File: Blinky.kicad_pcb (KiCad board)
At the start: 2 copper layers, 35.6 x 26.7 mm, 7 parts, among them U1 7555

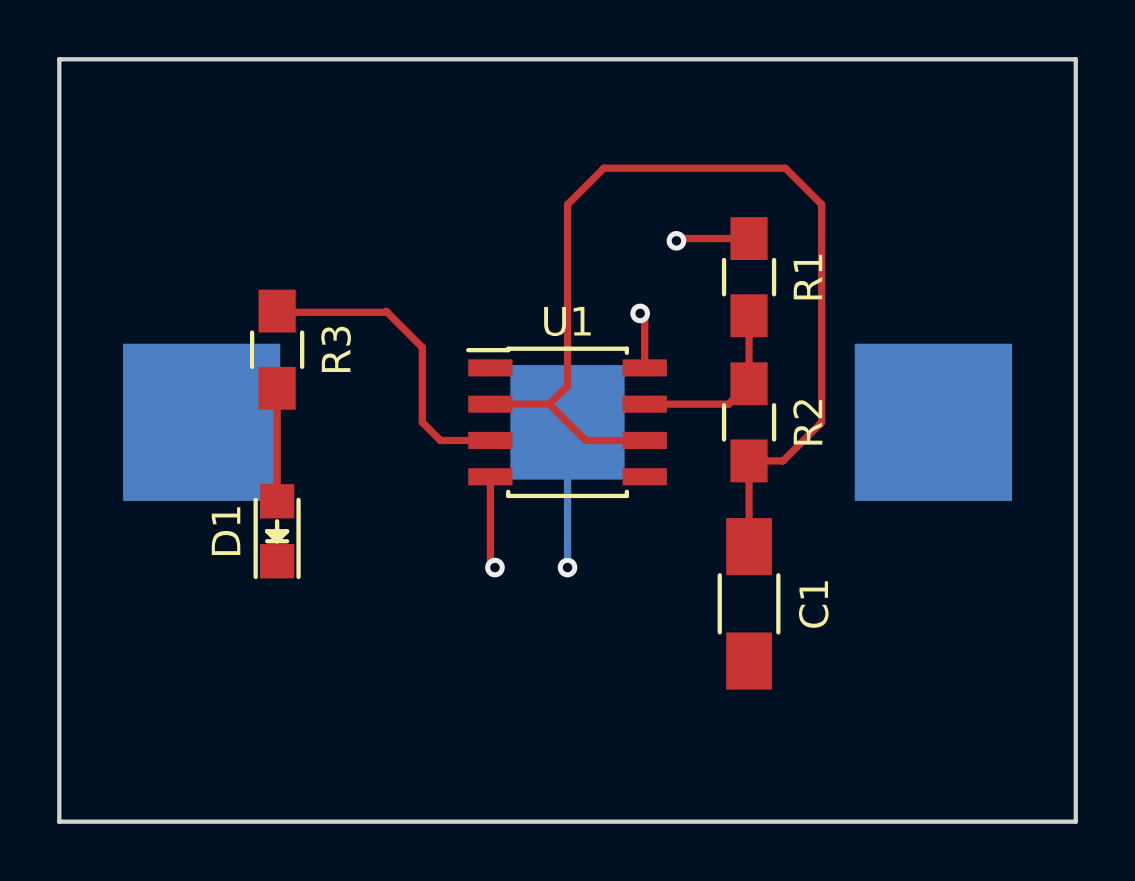
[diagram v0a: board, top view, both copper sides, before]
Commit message: Fix capacitor footprint - should have been 0805
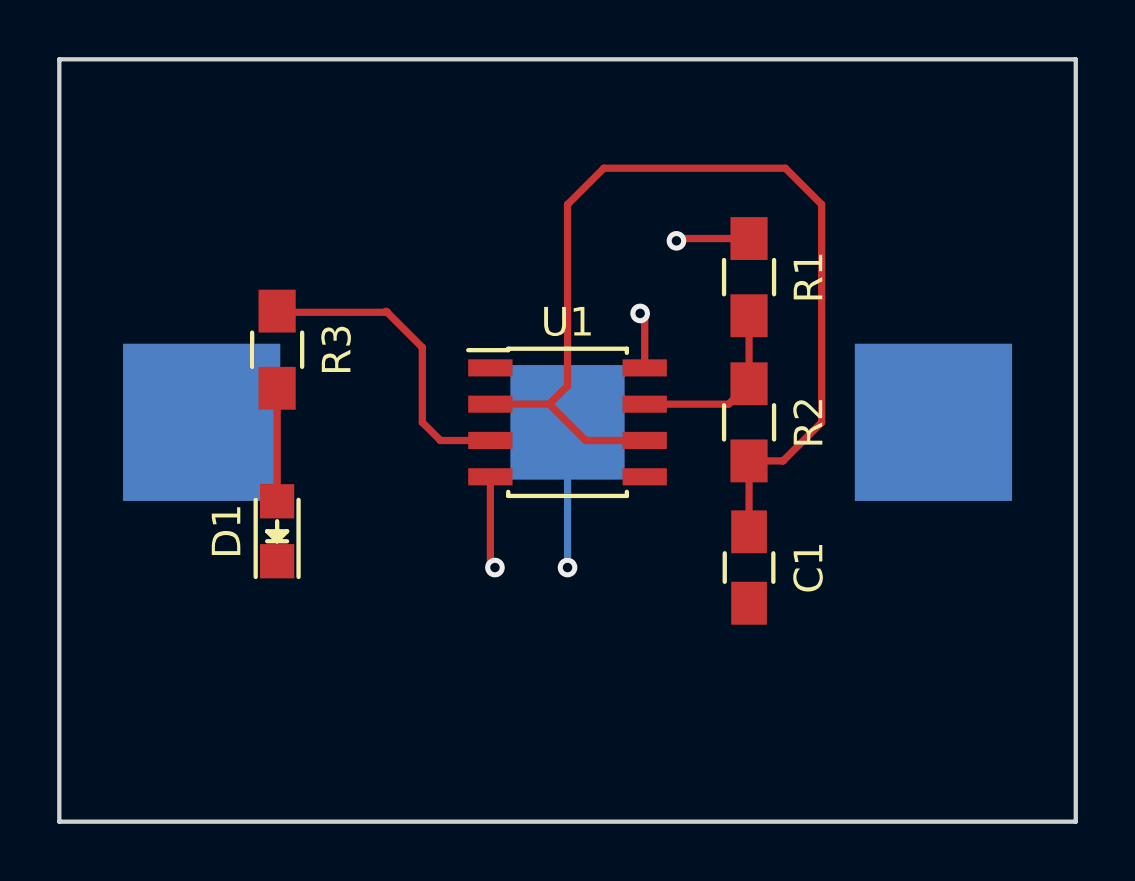
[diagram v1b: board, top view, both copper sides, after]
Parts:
- C1: footprint Capacitors_SMD:C_1206_HandSoldering -> Capacitors_SMD:C_0805_HandSoldering
- moved C1 1.27 mm to (162.6, 123.2)
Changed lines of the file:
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@@
   (layers
     (0 F.Cu mixed)
-    (31 B.Cu mixed)
+    (31 B.Cu mixed hide)
     (32 B.Adhes user)
     (33 F.Adhes user)
@@
     (add_net "Net-(U1-Pad5)")
   )
-  (module Capacitors_SMD:C_1206_HandSoldering (layer F.Cu)
-    (at 162.56 124.46 270)
-    (descr "Capacitor SMD 1206, hand soldering")
-    (tags "capacitor 1206")
-    (attr smd)
-    (fp_text reference C1 (at 0 -2.3 270) (layer F.SilkS)
-      (effects (font (size 1 1) (thickness 0.15)))
-    )
-    (fp_text value 1U (at 0 2.3 270) (layer F.Fab)
-      (effects (font (size 1 1) (thickness 0.15)))
-    )
-    (fp_line (start -3.3 -1.15) (end 3.3 -1.15) (layer F.CrtYd) (width 0.05))
-    (fp_line (start -3.3 1.15) (end 3.3 1.15) (layer F.CrtYd) (width 0.05))
-    (fp_line (start -3.3 -1.15) (end -3.3 1.15) (layer F.CrtYd) (width 0.05))
-    (fp_line (start 3.3 -1.15) (end 3.3 1.15) (layer F.CrtYd) (width 0.05))
-    (fp_line (start 1 -1.025) (end -1 -1.025) (layer F.SilkS) (width 0.15))
-    (fp_line (start -1 1.025) (end 1 1.025) (layer F.SilkS) (width 0.15))
-    (pad 1 smd rect (at -2 0 270) (size 2 1.6) (layers F.Cu F.Paste F.Mask)
-      (net 1 "Net-(C1-Pad1)"))
-    (pad 2 smd rect (at 2 0 270) (size 2 1.6) (layers F.Cu F.Paste F.Mask)
-      (net 2 GND))
-    (model Capacitors_SMD.3dshapes/C_1206_HandSoldering.wrl
-      (at (xyz 0 0 0))
-      (scale (xyz 1 1 1))
-      (rotate (xyz 0 0 0))
-    )
-  )
   (module LEDs:LED_0805 (layer F.Cu)
     (at 146.05 121.92 90)
@@
       (net 4 /VDD))
   )
+  (module Capacitors_SMD:C_0805_HandSoldering (layer F.Cu)
+    (at 162.56 123.19 270)
+    (descr "Capacitor SMD 0805, hand soldering")
+    (tags "capacitor 0805")
+    (attr smd)
+    (fp_text reference C1 (at 0 -2.1 270) (layer F.SilkS)
+      (effects (font (size 1 1) (thickness 0.15)))
+    )
+    (fp_text value 1U (at 0 2.1 270) (layer F.Fab)
+      (effects (font (size 1 1) (thickness 0.15)))
+    )
+    (fp_line (start -1 0.625) (end -1 -0.625) (layer F.Fab) (width 0.15))
+    (fp_line (start 1 0.625) (end -1 0.625) (layer F.Fab) (width 0.15))
+    (fp_line (start 1 -0.625) (end 1 0.625) (layer F.Fab) (width 0.15))
+    (fp_line (start -1 -0.625) (end 1 -0.625) (layer F.Fab) (width 0.15))
+    (fp_line (start -2.3 -1) (end 2.3 -1) (layer F.CrtYd) (width 0.05))
+    (fp_line (start -2.3 1) (end 2.3 1) (layer F.CrtYd) (width 0.05))
+    (fp_line (start -2.3 -1) (end -2.3 1) (layer F.CrtYd) (width 0.05))
+    (fp_line (start 2.3 -1) (end 2.3 1) (layer F.CrtYd) (width 0.05))
+    (fp_line (start 0.5 -0.85) (end -0.5 -0.85) (layer F.SilkS) (width 0.15))
+    (fp_line (start -0.5 0.85) (end 0.5 0.85) (layer F.SilkS) (width 0.15))
+    (pad 1 smd rect (at -1.25 0 270) (size 1.5 1.25) (layers F.Cu F.Paste F.Mask)
+      (net 1 "Net-(C1-Pad1)"))
+    (pad 2 smd rect (at 1.25 0 270) (size 1.5 1.25) (layers F.Cu F.Paste F.Mask)
+      (net 2 GND))
+    (model Capacitors_SMD.3dshapes/C_0805_HandSoldering.wrl
+      (at (xyz 0 0 0))
+      (scale (xyz 1 1 1))
+      (rotate (xyz 0 0 0))
+    )
+  )
   (gr_line (start 173.99 132.08) (end 138.43 132.08) (angle 90) (layer Edge.Cuts) (width 0.15))
